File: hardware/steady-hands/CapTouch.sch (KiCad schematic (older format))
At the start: 5 parts, among them U4 CPT112S-A02-GM

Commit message: Updates files. Just making sure everything I didn't create any errors
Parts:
- C20: symbol Sij_Touch:CapSense_01x08 -> steady-hands:CapSense_01x08
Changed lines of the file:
@@
 $EndComp
 $Comp
-L Sij_Touch:CapSense_01x08 C20
+L steady-hands:CapSense_01x08 C20
 U 1 1 5EFBC936
 P 7550 4450
+AR Path="/5EFBC936" Ref="C20"  Part="1"
+AR Path="/5EFB8965/5EFBC936" Ref="C20"  Part="1"
 F 0 "C20" H 7878 5096 50  0000 L CNN
 F 1 "CapSense_01x08" H 7878 5005 50  0000 L CNN

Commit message: Adds footprints
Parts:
- C18, C19: footprint (none) -> Capacitor_SMD:C_0402_1005Metric
- R11: footprint (none) -> Resistor_SMD:R_0402_1005Metric
- U4: footprint (none) -> Sij_Sensors:CPT112S-A02-GM
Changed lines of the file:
@@
 $Descr A4 11693 8268
 encoding utf-8
-Sheet 4 7
+Sheet 3 6
 Title ""
 Date ""
@@
 F 0 "C18" H 3465 4046 50  0000 L CNN
 F 1 "4.7uF" H 3465 3955 50  0000 L CNN
-F 2 "" H 3388 3850 50  0001 C CNN
+F 2 "Capacitor_SMD:C_0402_1005Metric" H 3388 3850 50  0001 C CNN
 F 3 "~" H 3350 4000 50  0001 C CNN
 	1    3350 4000
@@
 F 0 "C19" H 3915 4046 50  0000 L CNN
 F 1 "0.1uF" H 3915 3955 50  0000 L CNN
-F 2 "" H 3838 3850 50  0001 C CNN
+F 2 "Capacitor_SMD:C_0402_1005Metric" H 3838 3850 50  0001 C CNN
 F 3 "~" H 3800 4000 50  0001 C CNN
 	1    3800 4000
@@
 F 0 "U4" H 6050 5500 50  0000 C CNN
 F 1 "CPT112S-A02-GM" H 6050 5400 50  0000 C CNN
-F 2 "" H 6050 5500 50  0001 C CNN
+F 2 "Sij_Sensors:CPT112S-A02-GM" H 6050 5500 50  0001 C CNN
 F 3 "https://www.mouser.com/datasheet/2/368/CPT112S-DataSheet-1397794.pdf" H 6050 5500 50  0001 C CNN
 	1    6050 5500
@@
 Wire Wire Line
 	5950 5100 6050 5100
-Wire Wire Line
-	6050 5100 6050 5200
-Connection ~ 6050 5100
-Wire Wire Line
-	6050 5100 6150 5100
 $Comp
 L Device:R R11
@@
 F 0 "R11" H 4920 3446 50  0000 L CNN
 F 1 "10k" H 4920 3355 50  0000 L CNN
-F 2 "" V 4780 3400 50  0001 C CNN
+F 2 "Resistor_SMD:R_0402_1005Metric" V 4780 3400 50  0001 C CNN
 F 3 "~" H 4850 3400 50  0001 C CNN
 	1    4850 3400
@@
 	1    0    0    -1
 $EndComp
+Wire Wire Line
+	6150 5100 6050 5100
+Connection ~ 6050 5100
+Wire Wire Line
+	6050 5200 6050 5100
 $EndSCHEMATC

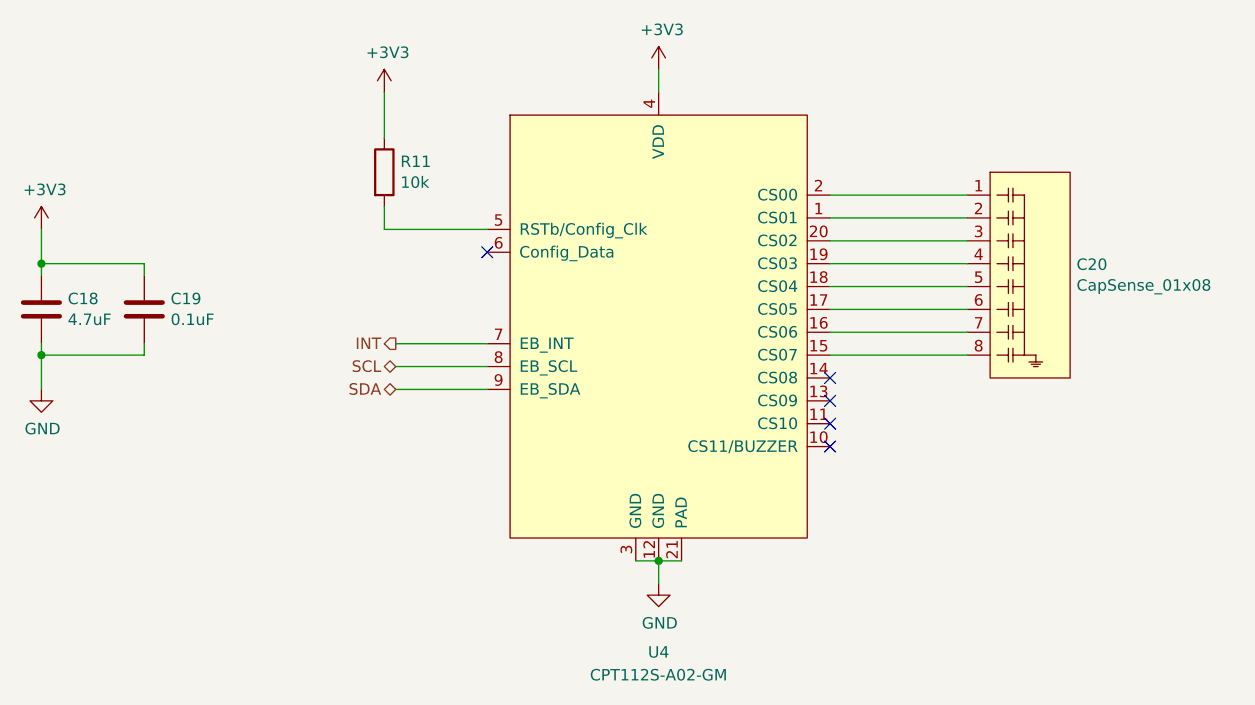
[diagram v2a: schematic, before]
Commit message: Edits PCB layout
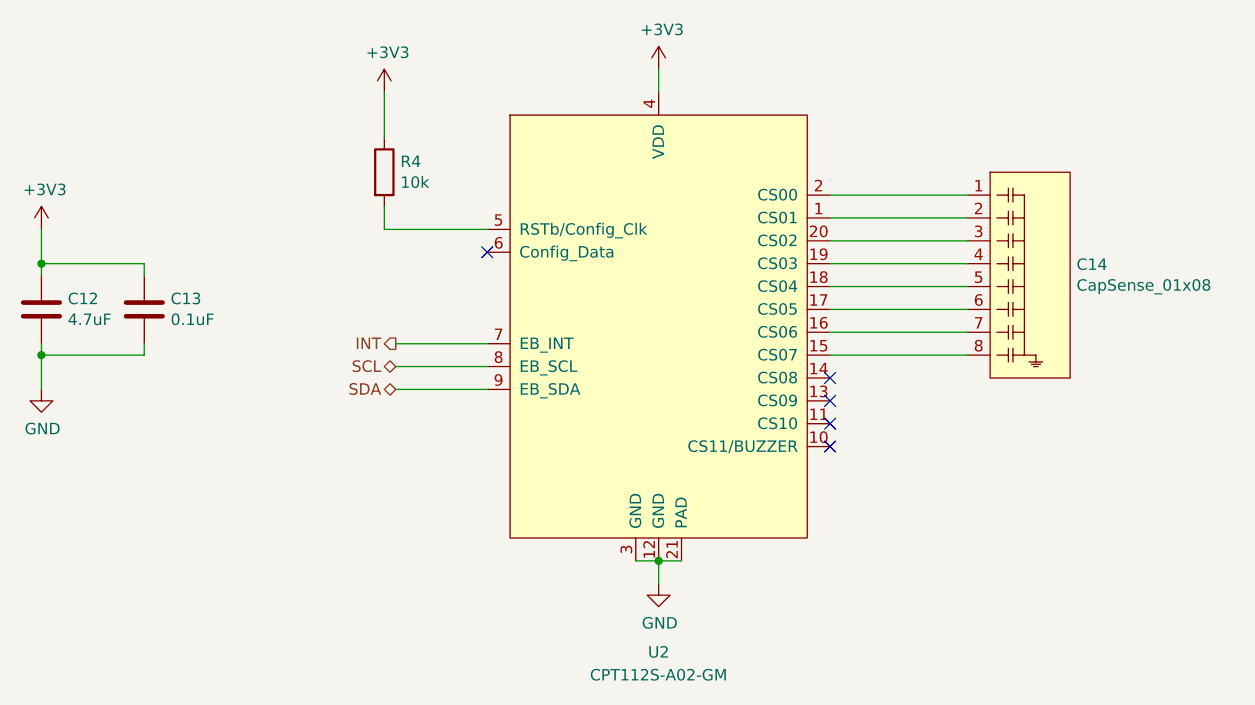
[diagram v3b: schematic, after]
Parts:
- renumbered C18 to C12, C19 to C13, C20 to C14, R11 to R4, U4 to U2
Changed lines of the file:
@@
 SDA
 $Comp
-L Device:C C18
+L Device:C C12
 U 1 1 5EF414DE
 P 3350 4000
-F 0 "C18" H 3465 4046 50  0000 L CNN
+F 0 "C12" H 3465 4046 50  0000 L CNN
 F 1 "4.7uF" H 3465 3955 50  0000 L CNN
 F 2 "Capacitor_SMD:C_0402_1005Metric" H 3388 3850 50  0001 C CNN
@@
 $EndComp
 $Comp
-L Device:C C19
+L Device:C C13
 U 1 1 5EF4247D
 P 3800 4000
-F 0 "C19" H 3915 4046 50  0000 L CNN
+F 0 "C13" H 3915 4046 50  0000 L CNN
 F 1 "0.1uF" H 3915 3955 50  0000 L CNN
 F 2 "Capacitor_SMD:C_0402_1005Metric" H 3838 3850 50  0001 C CNN
@@
 $EndComp
 $Comp
-L steady-hands:CapSense_01x08 C20
+L steady-hands:CapSense_01x08 C?
 U 1 1 5EFBC936
 P 7550 4450
-AR Path="/5EFBC936" Ref="C20"  Part="1"
-AR Path="/5EFB8965/5EFBC936" Ref="C20"  Part="1"
-F 0 "C20" H 7878 5096 50  0000 L CNN
+AR Path="/5EFBC936" Ref="C?"  Part="1"
+AR Path="/5EFB8965/5EFBC936" Ref="C14"  Part="1"
+F 0 "C14" H 7878 5096 50  0000 L CNN
 F 1 "CapSense_01x08" H 7878 5005 50  0000 L CNN
 F 2 "Sij_Touch:TouchSlider-8_35x10mm" H 7550 4450 50  0001 C CNN
@@
 $EndComp
 $Comp
-L power:GND #PWR0132
+L power:GND #PWR029
 U 1 1 5EF589C1
 P 6050 5200
-F 0 "#PWR0132" H 6050 4950 50  0001 C CNN
+F 0 "#PWR029" H 6050 4950 50  0001 C CNN
 F 1 "GND" H 6055 5027 50  0000 C CNN
 F 2 "" H 6050 5200 50  0001 C CNN
@@
 	3350 4200 3350 4350
 $Comp
-L power:GND #PWR0133
+L power:GND #PWR026
 U 1 1 5EF5D4FE
 P 3350 4350
-F 0 "#PWR0133" H 3350 4100 50  0001 C CNN
+F 0 "#PWR026" H 3350 4100 50  0001 C CNN
 F 1 "GND" H 3355 4177 50  0000 C CNN
 F 2 "" H 3350 4350 50  0001 C CNN
@@
 Connection ~ 3350 4200
 $Comp
-L steady-hands:CPT112S-A02-GM U4
+L steady-hands:CPT112S-A02-GM U2
 U 1 1 5EF85C6E
 P 6050 5500
-F 0 "U4" H 6050 5500 50  0000 C CNN
+F 0 "U2" H 6050 5500 50  0000 C CNN
 F 1 "CPT112S-A02-GM" H 6050 5400 50  0000 C CNN
 F 2 "Sij_Sensors:CPT112S-A02-GM" H 6050 5500 50  0001 C CNN
@@
 	5950 5100 6050 5100
 $Comp
-L Device:R R11
+L Device:R R4
 U 1 1 5EF98D5D
 P 4850 3400
-F 0 "R11" H 4920 3446 50  0000 L CNN
+F 0 "R4" H 4920 3446 50  0000 L CNN
 F 1 "10k" H 4920 3355 50  0000 L CNN
 F 2 "Resistor_SMD:R_0402_1005Metric" V 4780 3400 50  0001 C CNN
@@
 	6050 3050 6050 2950
 $Comp
-L power:+3V3 #PWR0134
+L power:+3V3 #PWR028
 U 1 1 5F161753
 P 6050 2950
-F 0 "#PWR0134" H 6050 2800 50  0001 C CNN
+F 0 "#PWR028" H 6050 2800 50  0001 C CNN
 F 1 "+3V3" H 6065 3123 50  0000 C CNN
 F 2 "" H 6050 2950 50  0001 C CNN
@@
 $EndComp
 $Comp
-L power:+3V3 #PWR0135
+L power:+3V3 #PWR027
 U 1 1 5F1618F5
 P 4850 3050
-F 0 "#PWR0135" H 4850 2900 50  0001 C CNN
+F 0 "#PWR027" H 4850 2900 50  0001 C CNN
 F 1 "+3V3" H 4865 3223 50  0000 C CNN
 F 2 "" H 4850 3050 50  0001 C CNN
@@
 $EndComp
 $Comp
-L power:+3V3 #PWR0136
+L power:+3V3 #PWR025
 U 1 1 5F161AA4
 P 3350 3650
-F 0 "#PWR0136" H 3350 3500 50  0001 C CNN
+F 0 "#PWR025" H 3350 3500 50  0001 C CNN
 F 1 "+3V3" H 3365 3823 50  0000 C CNN
 F 2 "" H 3350 3650 50  0001 C CNN
